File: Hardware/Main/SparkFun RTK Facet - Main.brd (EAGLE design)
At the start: 59 x 43 mm, 126 parts, among them J1 QWIIC_RIGHT_ANGLE, J2 U.FL, J9 CORTEX_JTAG_DEBUG_PTH, Q2 MBT3904DW1T1, Q3 SIL2308, U1 74HC4052D, U10 MCP73833, U12 AP2112K-3.3, U2 3.3V, U3 U-BLOX_ZED-F9P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

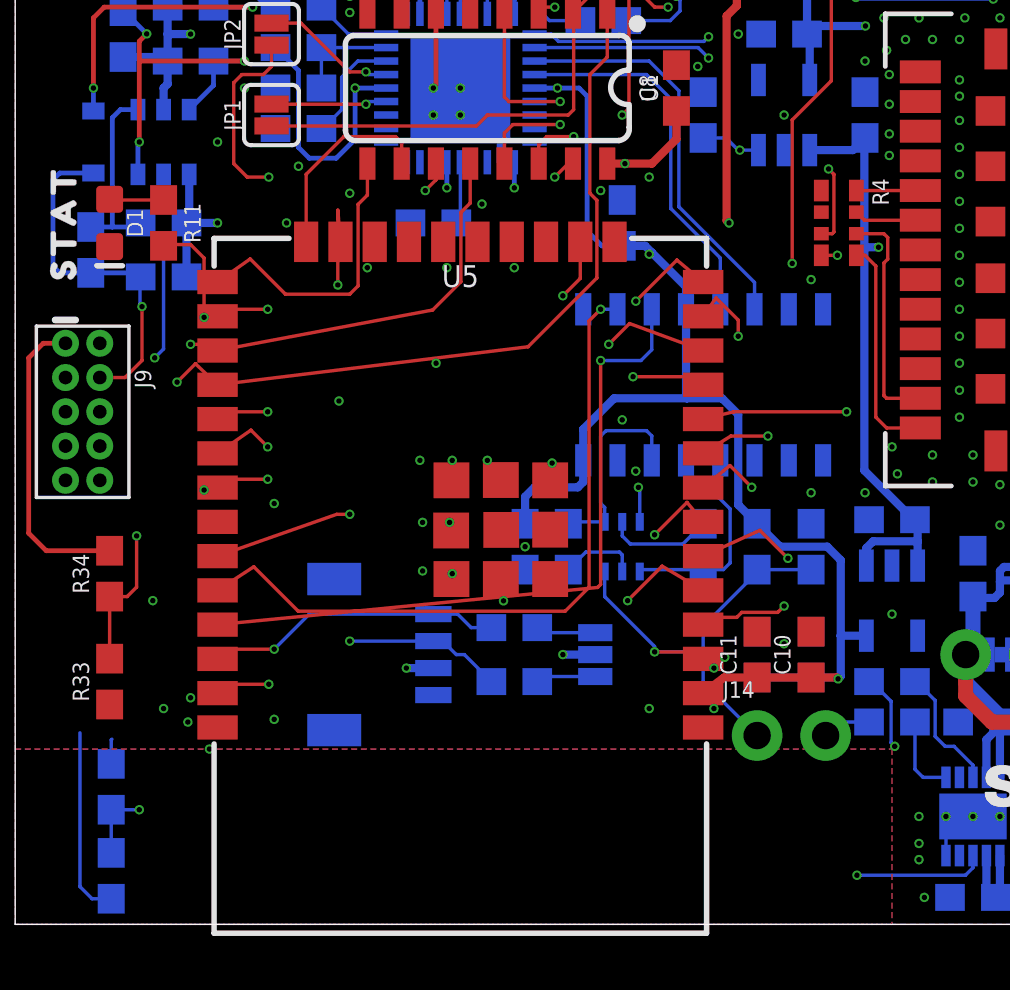
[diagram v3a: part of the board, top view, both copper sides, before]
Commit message: Update ESP32 to larger FP.
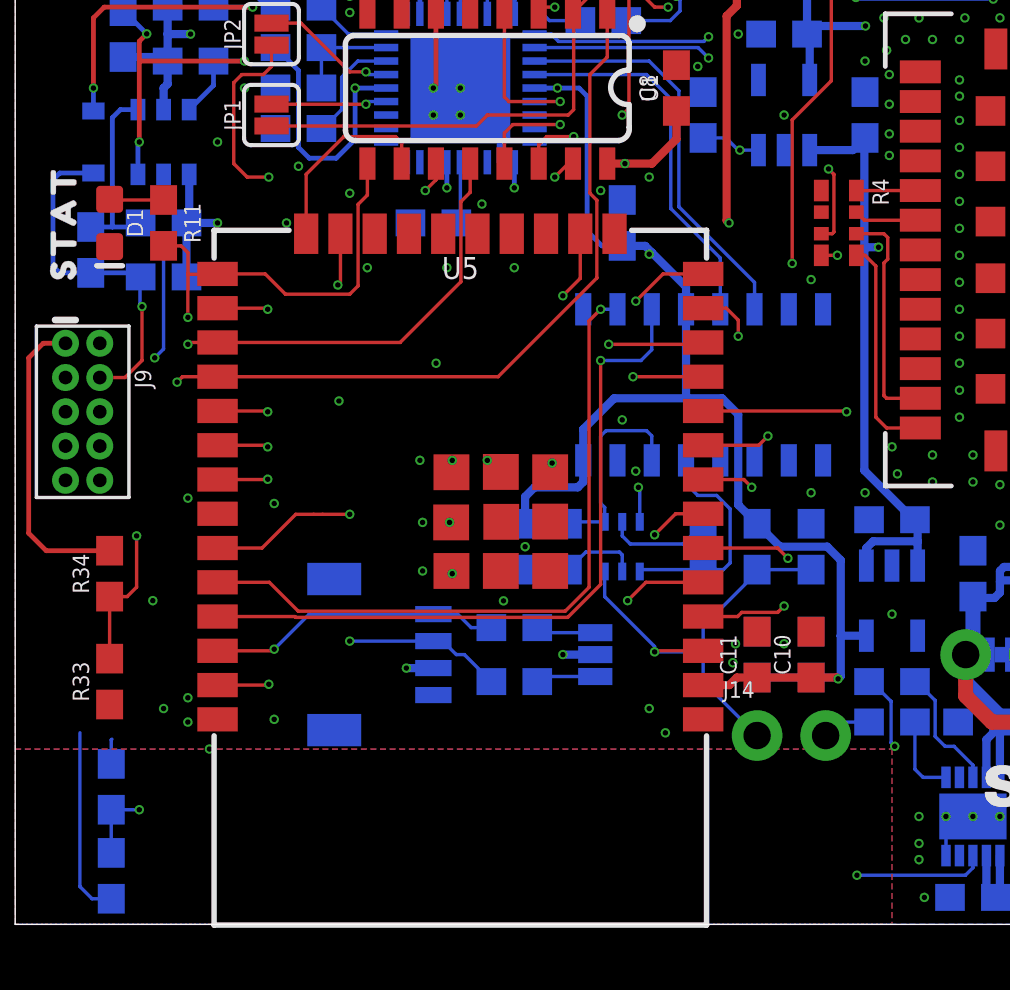
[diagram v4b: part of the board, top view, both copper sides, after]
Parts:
- moved U5 0.30 mm to (16.5, 15.3)
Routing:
- net ESP_15/MTDO/RADIO_!RESET!: track 46.2 -> 44.2 mm
- net ESP_0/BOOT/STAT_LED/MUX_B: track 39.2 -> 40.1 mm
- net ESP_16/ZED-TXO1: track 83.4 -> 83.9 mm
- net ESP_I35/DEVICE_SENSE: track 27.9 -> 27.4 mm
- net ESP_14/PERIPHERAL_POWER/MTMS: track 35.6 -> 35.0 mm
- net ESP_12/MTDI: track 27.8 -> 27.3 mm
- net ESP_32/RADIO_TXO: track 23.6 -> 23.1 mm
- net ESP_18/SD_SCK: track 52.9 -> 52.4 mm

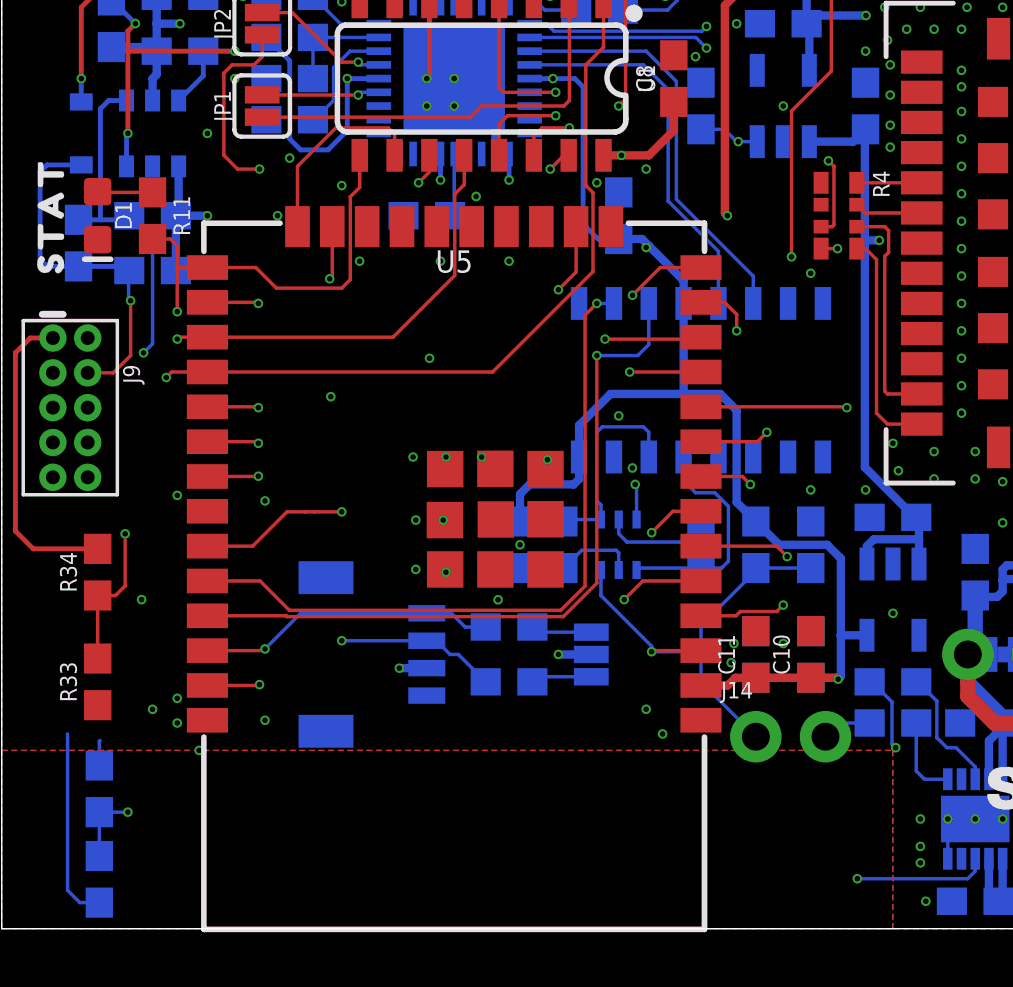
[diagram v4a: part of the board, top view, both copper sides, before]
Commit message: Adjust ESP32 FP.
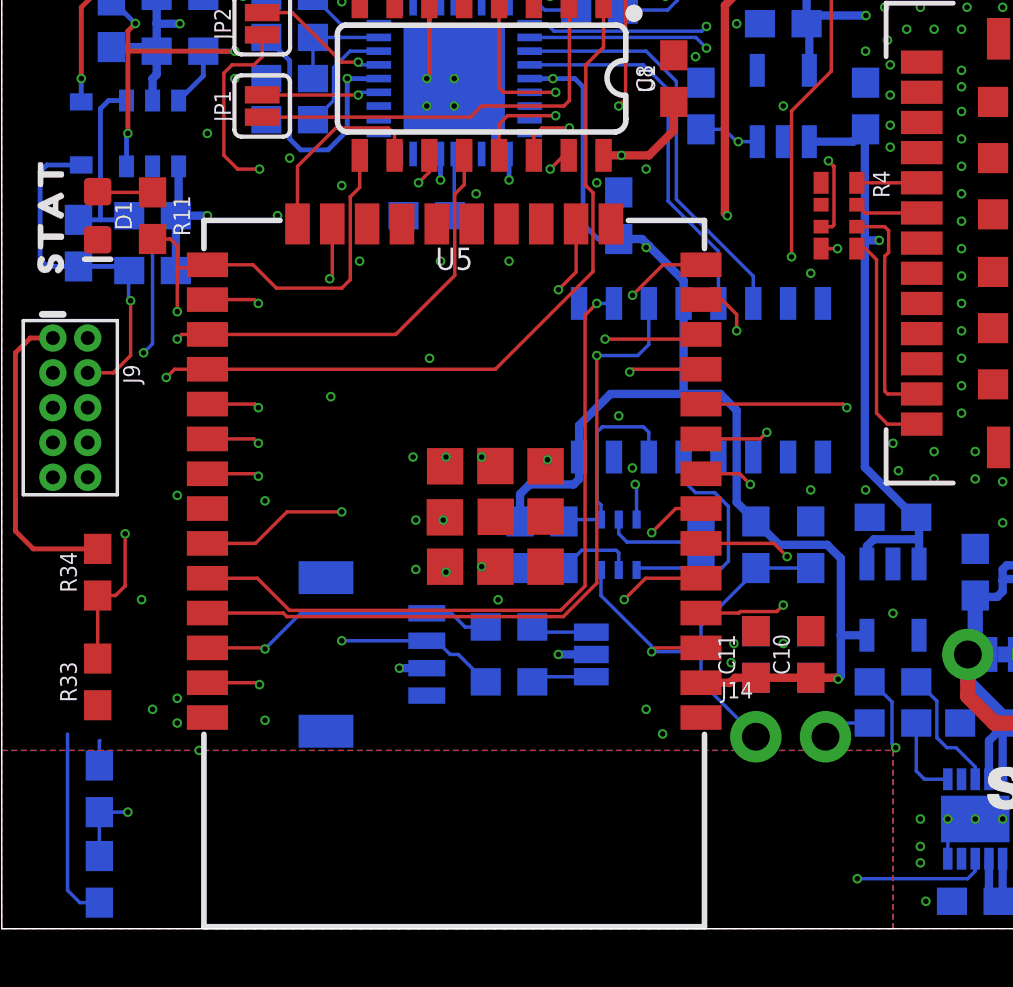
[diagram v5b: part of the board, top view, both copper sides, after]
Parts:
- moved U5 0.10 mm to (16.5, 15.4)

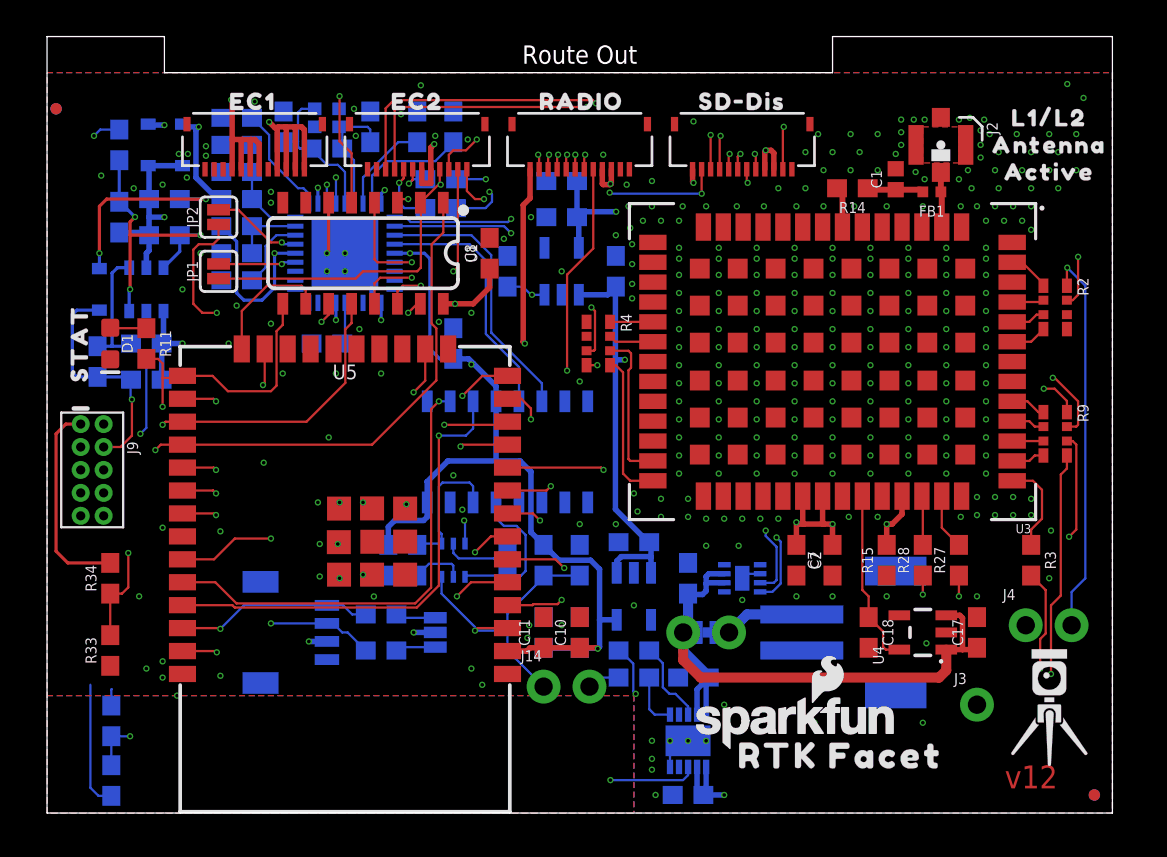
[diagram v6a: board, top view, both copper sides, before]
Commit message: Add I2C test header to display board - v1.6
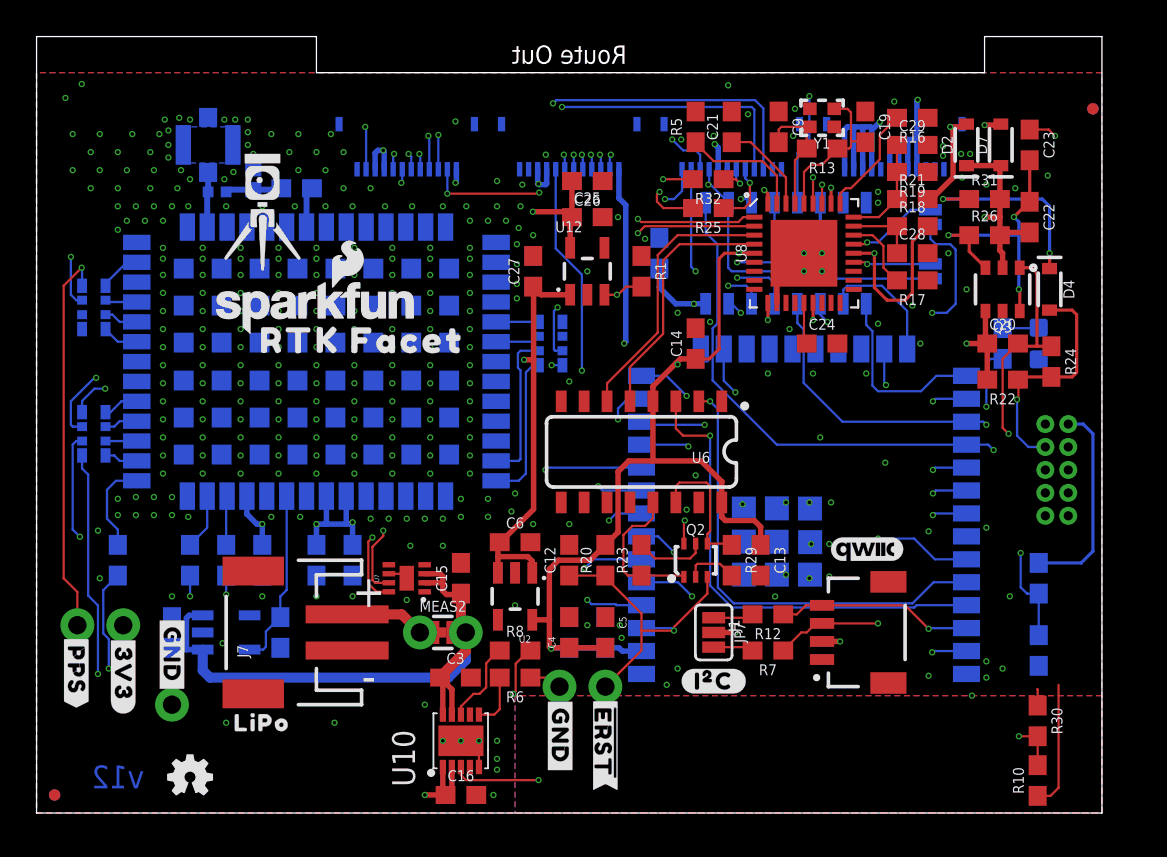
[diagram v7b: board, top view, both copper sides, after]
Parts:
- moved FRAME1 106.7 mm to (-24.1, 6.35), flipped to the bottom
- moved FRAME2 106.7 mm to (-24.1, 6.35), flipped to the bottom
- moved U$2 66.7 mm to (-4.12, 81.3), flipped to the bottom
- moved JP21 57.6 mm to (0.42, 1.00), flipped to the bottom
- moved JP71 57.6 mm to (0.42, 1.00), flipped to the top
- moved JP61 57.4 mm to (57.9, 39.0), flipped to the bottom
- moved JP81 57.4 mm to (57.9, 39.0), flipped to the top
- moved U$10 55.2 mm to (1.62, 7.90), flipped to the top
- moved U$24 54.8 mm to (56.6, 26.0), flipped to the bottom
- moved J9 53.4 mm to (55.9, 19.0), flipped to the bottom
- moved R2 53.2 mm to (2.62, 28.0), flipped to the bottom
- moved R9 53.2 mm to (2.62, 21.0), flipped to the bottom
- moved R24 52.8 mm to (55.6, 25.0), flipped to the top
- moved D4 52.6 mm to (55.5, 29.0), flipped to the top
- moved U$15 52.6 mm to (2.91, 5.84), flipped to the bottom
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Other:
- outline, holes or cut-outs redrawn

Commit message: Facet v13: change charger IC FP, discrete 33s, change cream on ESP32.
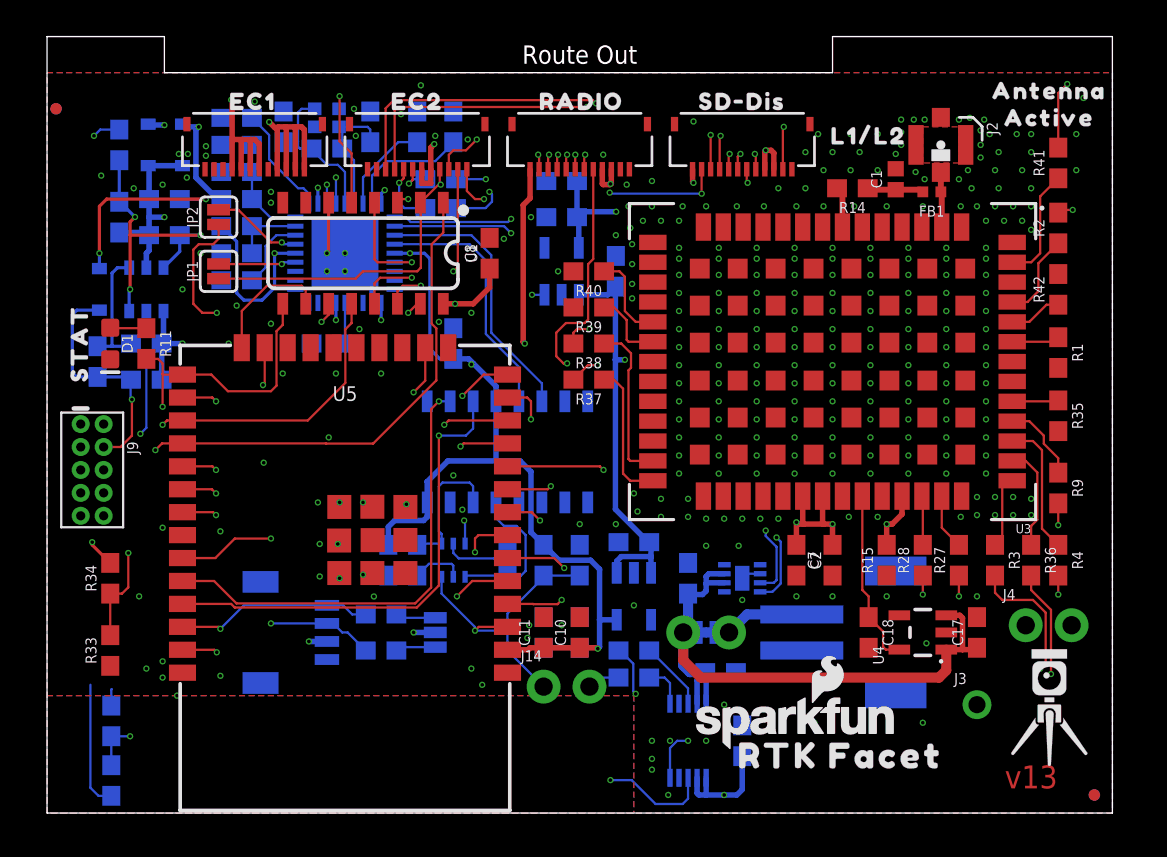
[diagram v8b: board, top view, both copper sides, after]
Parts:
- added R35, R36, R37, R38, R39, R40, R41, R42: 33, SparkFun-Resistors:0603
- JP1, JP2: value (none) -> JUMPER-SMT_2_NO_SILK
- MEAS2: value (none) -> JUMPER-COMBO_2_NC_TRACE
- R1: value 100k -> 33
- R2, R4, R9: device SparkFun-Resistors:1206_RA -> SparkFun-Resistors:0603
- R25, R32: value 22 -> 22Ω
- U10: value MCP73833 -> MCP73833MSOP; device SparkFun-IC-Power:DFN-10 -> SparkFun-IC-Power:MSOP10
- U12: value AP2112K-3.3 -> AP2112K-3.3V
- U2: value 3.3V -> AP2112K-3.3V
- U5: value ESP-WROOM-3232D -> ESP-WROOM-3232D-DFMP; device SparkFun-RF:ESP-WROOM-32D -> SparkFun-RF:ESP-WROOM-32D-DFM_PASTE
- moved FRAME1 106.7 mm to (82.5, 6.35), flipped to the top
- moved FRAME2 106.7 mm to (82.5, 6.35), flipped to the top
- moved U$2 66.7 mm to (62.5, 81.3), flipped to the top
- moved JP21 57.6 mm to (58.0, 1.00), flipped to the top
- moved JP71 57.6 mm to (58.0, 1.00), flipped to the bottom
- moved JP61 57.4 mm to (0.50, 39.0), flipped to the top
- moved JP81 57.4 mm to (0.50, 39.0), flipped to the bottom
- moved U$10 55.2 mm to (56.8, 7.90), flipped to the bottom
- moved U$24 54.8 mm to (1.80, 26.0), flipped to the top
- moved R2 53.6 mm to (56.0, 32.4), flipped to the top, turned to 90 degrees
- moved R9 53.5 mm to (56.0, 18.0), flipped to the top
- moved J9 53.4 mm to (2.50, 19.0), flipped to the top
- moved R24 52.8 mm to (2.80, 25.0), flipped to the bottom
- moved U$5 52.7 mm to (55.5, 38.5), flipped to the top
- moved U$7 52.7 mm to (55.5, 40.0), flipped to the top
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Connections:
- net ESP_14/PERIPHERAL_POWER/MTMS: no longer R1.2
- net ESP_17/ZED-RXI1: now also R36.2; no longer R9.P5
- net ESP_21/SDA: now also R4.2; no longer R9.P6
- net ESP_22/SCL: now also R9.2; no longer R9.P7
- net FENCE_LV: now also R40.1; no longer R4.P8
- net GND: no longer R1.1, U10.11
- net N$16: now also R1.1; no longer R2.P4
- net N$18: now also R42.1; no longer R2.P3
- net N$22: now also R35.1; no longer R9.P1
- net N$5: now also R2.1; no longer R2.P2
- net PPS: now also R41.1; no longer R2.P1
- net RTK_LV: now also R39.1; no longer R4.P7
- net RX2_LV: now also R38.1; no longer R4.P6
- net RXLV: now also R36.1; no longer R9.P4
- net SCL_LV: now also R9.1; no longer R9.P2
- net SDA_LV: now also R4.1; no longer R9.P3
- net TX2_LV: now also R37.1; no longer R4.P5
- net ZED-RXI2: now also R38.2; no longer R4.P3
- net ZED-TXO2: now also R37.2; no longer R4.P4
- net ZED_!RESET!: now also R1.2; no longer R2.P5
- net ZED_!SAFE!: now also R42.2; no longer R2.P6
- net ZED_EXTINT: now also R2.2; no longer R2.P7
- net ZED_FENCE_STAT: now also R40.2; no longer R4.P1
- net ZED_PPS_STAT: now also R41.2; no longer R2.P8
- net ZED_RTK_STAT: now also R39.2; no longer R4.P2
- net ZED_TX_READY: now also R35.2; no longer R9.P8
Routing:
- net ZED_TX_READY: track 12.8 -> 0.00 mm, vias 2 -> 0
- net ESP_22/SCL: track 141.2 -> 130.6 mm, vias 10 -> 9
- net ESP_17/ZED-RXI1: track 102.8 -> 96.3 mm
- net SDA_LV: track 1.73 -> 7.48 mm
- net ZED_EXTINT: track 59.2 -> 54.7 mm
- net ZED_PPS_STAT: track 80.8 -> 85.0 mm, vias 4 -> 3
- net PPS: track 2.34 -> 6.32 mm
- net RXLV: track 1.85 -> 5.81 mm
- net N$5: track 1.77 -> 4.80 mm
- net SCL_LV: track 1.85 -> 4.46 mm
- net FENCE_LV: track 2.37 -> 4.97 mm
- net ESP_21/SDA: track 140.4 -> 137.8 mm
- net ESP_16/ZED-TXO1: track 83.9 -> 85.8 mm
- net V_RAW: track 77.2 -> 79.1 mm
- net RTK_LV: track 2.49 -> 4.13 mm
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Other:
- outline, holes or cut-outs redrawn
- board text added: "Finish: ENIG"
- board text added: "Material: TG155"
- board text added: "Soldermask: Red"
- board text added: "Stackup: JLC7628 Impedence Controlled"
- board text added: "v13"
- board text removed: "Impedance controlled: JLC7628"
- board text removed: "v12"
